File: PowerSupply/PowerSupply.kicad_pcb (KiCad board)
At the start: 2 copper layers, 34.9 x 22.9 mm, 26 parts, among them IC1 MCP73832T-2DCI_OT, J1 Conn_01x04_Male, J2 Barrel_Jack, Q1 DMP2045U-7, SW1 SW_SPST, U1 AP3012, U2 AP3012

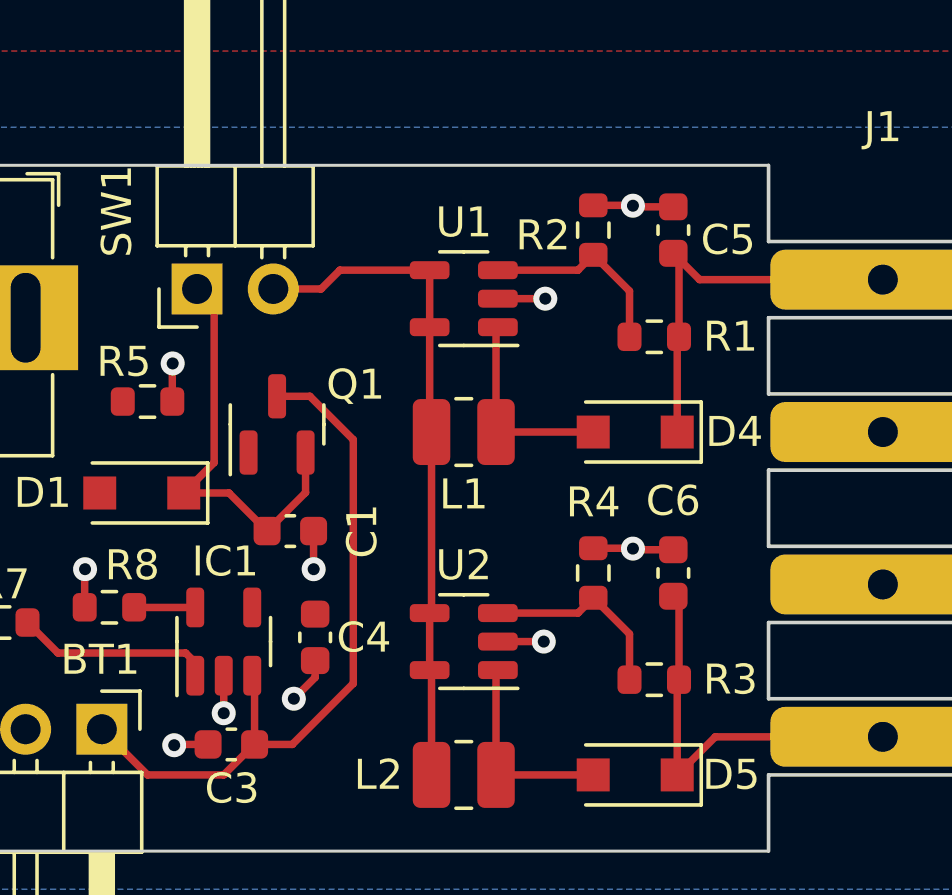
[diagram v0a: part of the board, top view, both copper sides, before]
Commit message: Moved capacitors for regulators to other side of power switch.
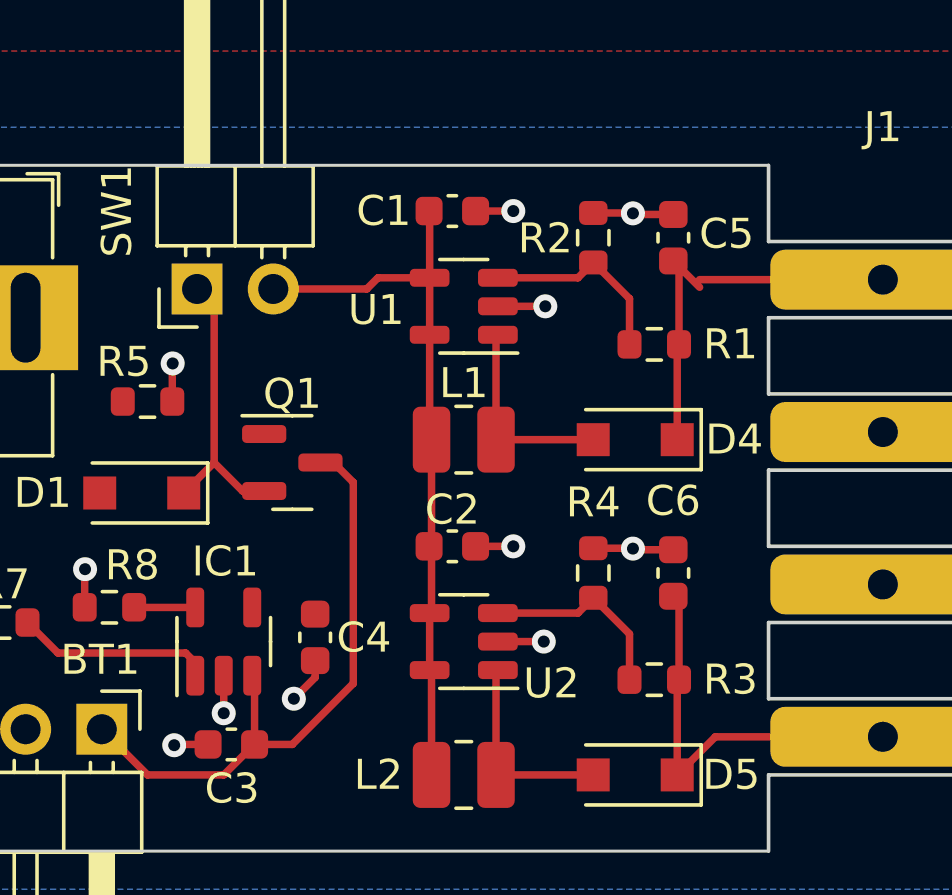
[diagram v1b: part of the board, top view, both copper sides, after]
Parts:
- added C2: 1uF, Capacitor_SMD:C_0603_1608Metric, F.Cu at (164.1, 77.5)
- moved C1 12.0 mm to (164.1, 66.3)
- moved Q1 1.37 mm to (158.8, 74.7), turned to 0 degrees
- moved C5 0.25 mm to (171.4, 67.2)
- moved D4 0.25 mm to (170.2, 73.9)
- moved L1 0.25 mm to (164.5, 73.9)
- moved R1 0.25 mm to (170.8, 70.7)
- moved R2 0.25 mm to (168.8, 67.2)
- moved U1 0.25 mm to (164.5, 69.5)
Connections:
- C1 pad 1: Net-(C1-Pad1) -> Net-(L1-Pad1)
- D1 pad 1: Net-(C1-Pad1) -> Net-(D1-Pad1)
- L1 pad 1: Net-(L2-Pad1) -> Net-(L1-Pad1)
- L2 pad 1: Net-(L2-Pad1) -> Net-(L1-Pad1)
- Q1 pad 2: Net-(C1-Pad1) -> Net-(D1-Pad1)
- SW1 pad 1: Net-(C1-Pad1) -> Net-(D1-Pad1)
- SW1 pad 2: Net-(L2-Pad1) -> Net-(L1-Pad1)
- U1 pad 4: Net-(L2-Pad1) -> Net-(L1-Pad1)
- U1 pad 5: Net-(L2-Pad1) -> Net-(L1-Pad1)
- U2 pad 4: Net-(L2-Pad1) -> Net-(L1-Pad1)
- U2 pad 5: Net-(L2-Pad1) -> Net-(L1-Pad1)
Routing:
- net Net-(L1-Pad1): track 0.00 -> 24.5 mm
- net Net-(L2-Pad1): track 22.4 -> 0.00 mm
- net Net-(C1-Pad1): track 13.9 -> 0.00 mm
- net Net-(D1-Pad1): track 0.00 -> 9.52 mm
- net +BATT: track 23.9 -> 20.7 mm
- net GND: track 16.3 -> 17.5 mm, vias 10 -> 11
